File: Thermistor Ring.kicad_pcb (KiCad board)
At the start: 2 copper layers, 158.9 x 126.1 mm, 19 parts, among them J1 Conn_01x04_Socket, U1 TPS7A2018PDBVR, U2 MCP9808T-E/MC, U3 MCP9808T-E/MC, U4 MCP9808T-E/MC, U5 MCP9808T-E/MC, U6 MCP9808T-E/MC, U7 MCP9808T-E/MC

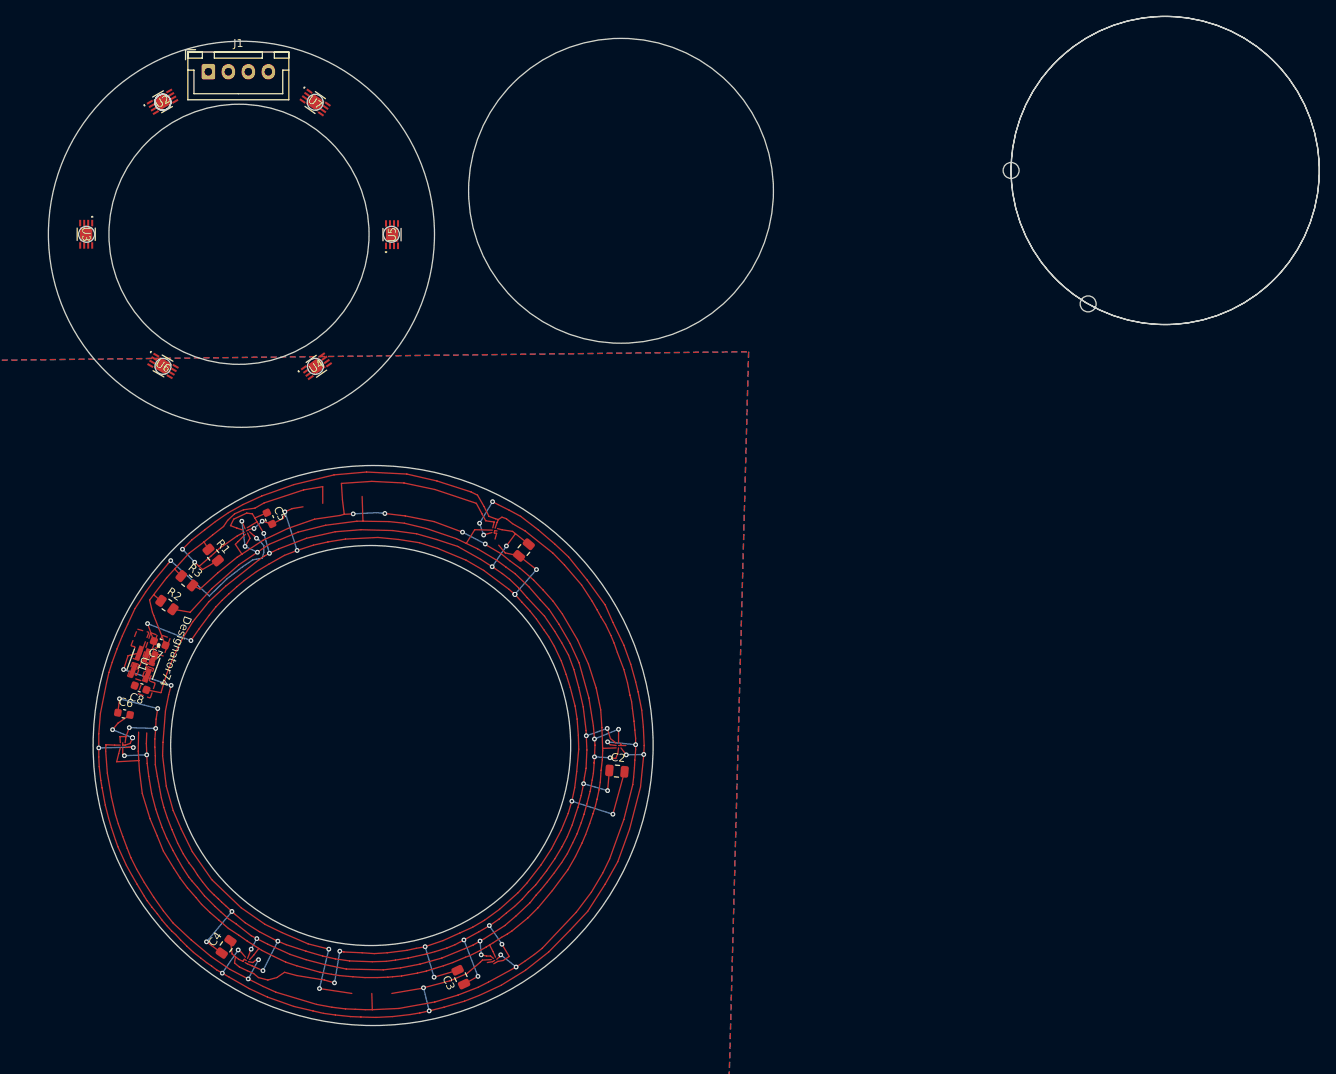
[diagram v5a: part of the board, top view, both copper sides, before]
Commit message: smaller ring first draft
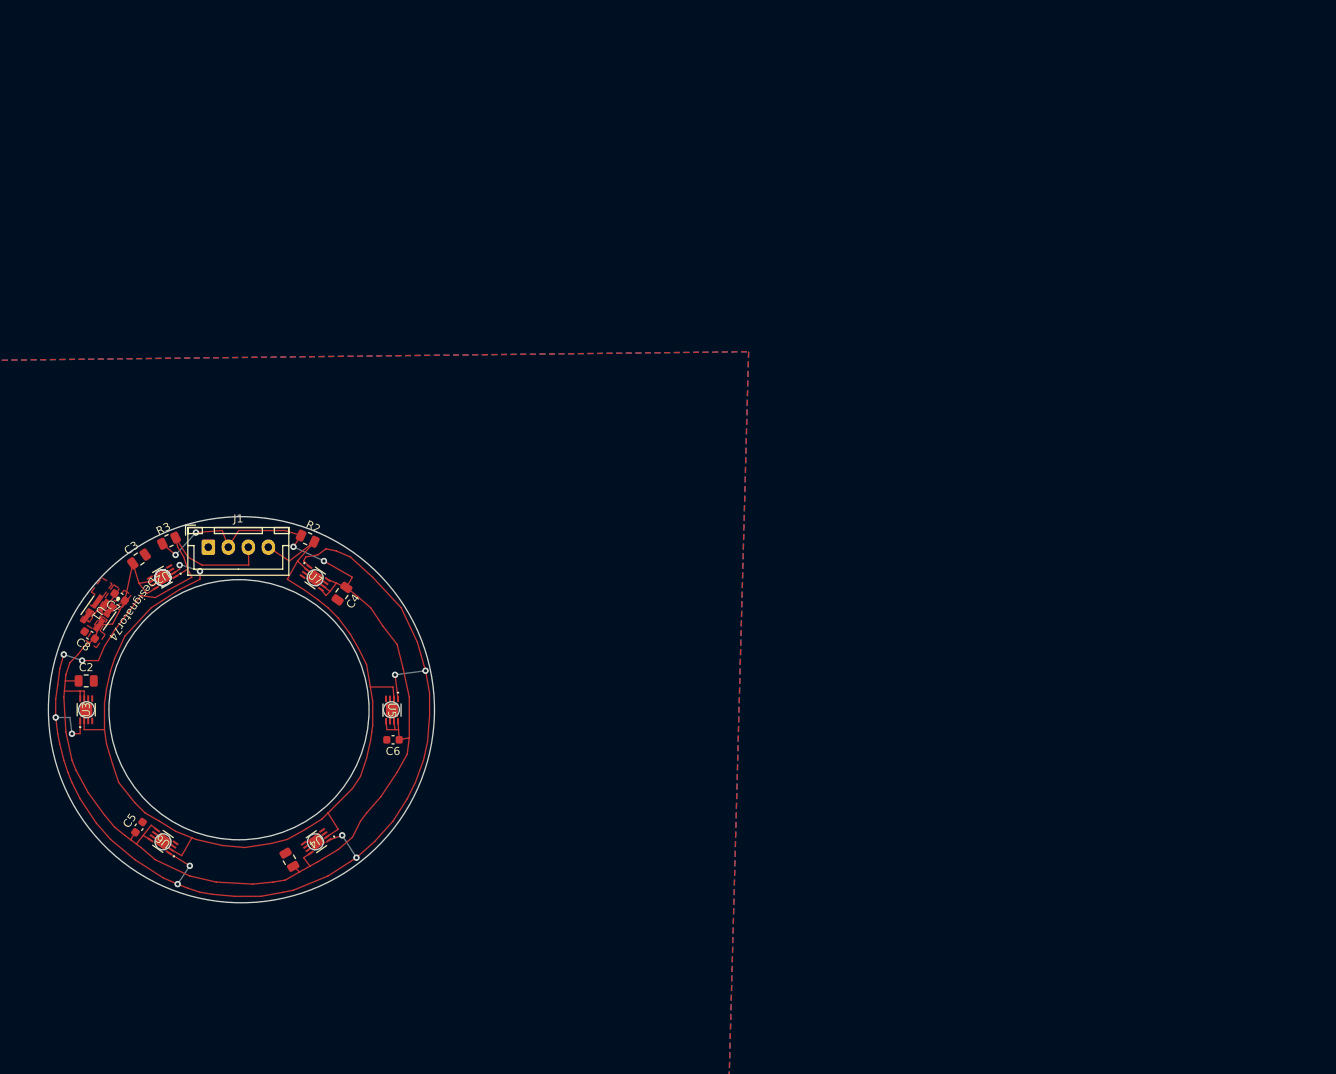
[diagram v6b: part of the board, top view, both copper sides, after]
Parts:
- removed R1: 4.7k, Resistor_SMD:R_0805_2012Metric
- moved C2 67.3 mm to (55.4, 52.1), turned to 0 degrees
- moved C3 66.0 mm to (62.0, 36.8), turned to 35 degrees
- moved U5 59.4 mm to (93.6, 55.7), turned to -90 degrees
- moved J1 59.4 mm to (70.6, 35.4)
- moved U2 59.4 mm to (64.9, 39.1), turned to -150 degrees
- moved U3 59.4 mm to (55.4, 55.7), turned to 90 degrees
- moved U6 59.4 mm to (65.0, 72.1), turned to 145 degrees
- moved U7 59.4 mm to (84.0, 39.2)
- moved U4 59.4 mm to (84.2, 72.2), turned to -145 degrees
- moved C1 48.6 mm to (80.8, 74.4), turned to 120 degrees
- moved C4 46.5 mm to (87.3, 41.2), turned to -125 degrees
- moved C5 41.9 mm to (62.0, 70.4), turned to 55 degrees
- moved C6 33.8 mm to (93.7, 59.4), turned to 180 degrees
- moved R2 19.4 mm to (83.1, 34.3), turned to -25 degrees
- moved C8 9.14 mm to (55.8, 46.3), turned to 145 degrees
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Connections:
- C5 pad 1: unconnected-(C5-Pad1) -> /Power 3.3-5V
- U2 pad 3: /INT -> unconnected-(U2-ALERT-Pad3)
- U3 pad 3: /INT -> unconnected-(U3-ALERT-Pad3)
- U4 pad 3: /INT -> unconnected-(U4-ALERT-Pad3)
- U5 pad 3: /INT -> unconnected-(U5-ALERT-Pad3)
- U6 pad 3: /INT -> unconnected-(U6-ALERT-Pad3)
- U7 pad 3: /INT -> unconnected-(U7-ALERT-Pad3)
- U7 pad 5: /SDA -> /Power 3.3-5V
- U7 pad 6: /SDA -> /Power 3.3-5V
- U7 pad 8: /SDA -> /Power 3.3-5V
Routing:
- net (no net): track 469.1 -> 0.00 mm, vias 13 -> 0
- net /INT: track 213.3 -> 0.00 mm, vias 8 -> 0
- net GND: track 195.9 -> 0.00 mm, vias 18 -> 0
- net /Power 3.3-5V: track 38.4 -> 179.9 mm, vias 20 -> 4
- net /SCL: track 196.8 -> 132.0 mm, vias 13 -> 2
- net /ENABLE: track 61.8 -> 0.00 mm, vias 4 -> 0
- net /SDA: track 202.3 -> 175.9 mm, vias 4 -> 10
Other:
- board size 158.9 x 126.1 mm -> 48.3 x 48.3 mm

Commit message: wip: some fixes
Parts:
- moved R3 0.98 mm to (66.5, 35.2), turned to -90 degrees
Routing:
- net /Power 3.3-5V: track 179.9 -> 192.3 mm, vias 4 -> 3
- net /SDA: track 175.9 -> 171.3 mm
- net /SCL: track 132.0 -> 128.0 mm
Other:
- outline, holes or cut-outs redrawn

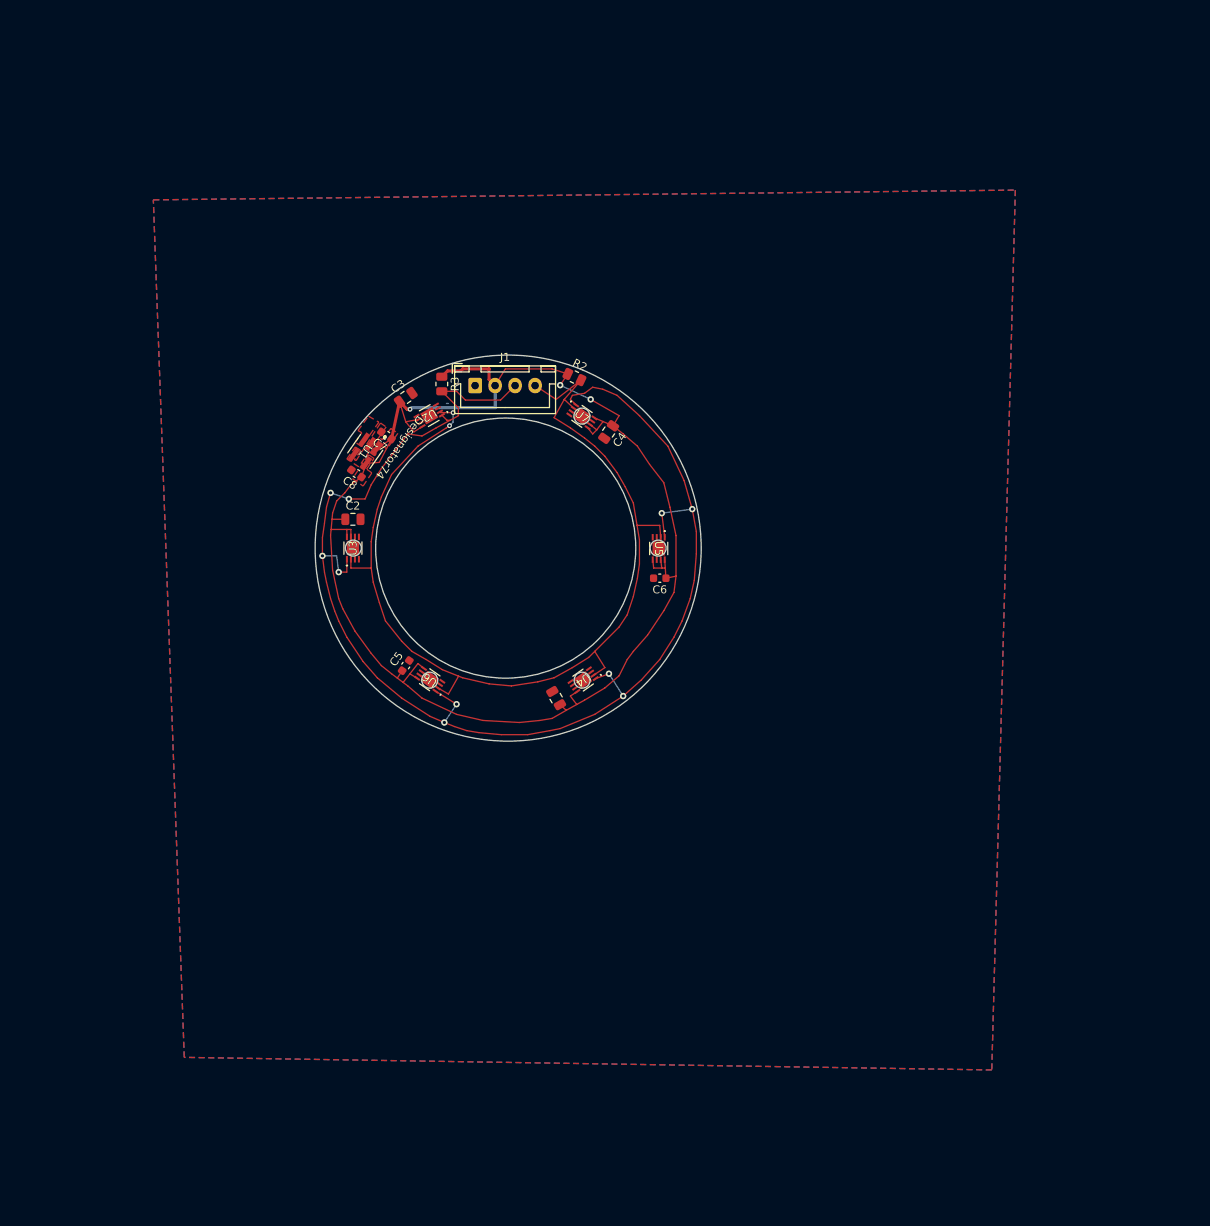
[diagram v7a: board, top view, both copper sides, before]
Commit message: Update PCB and resolve DRC
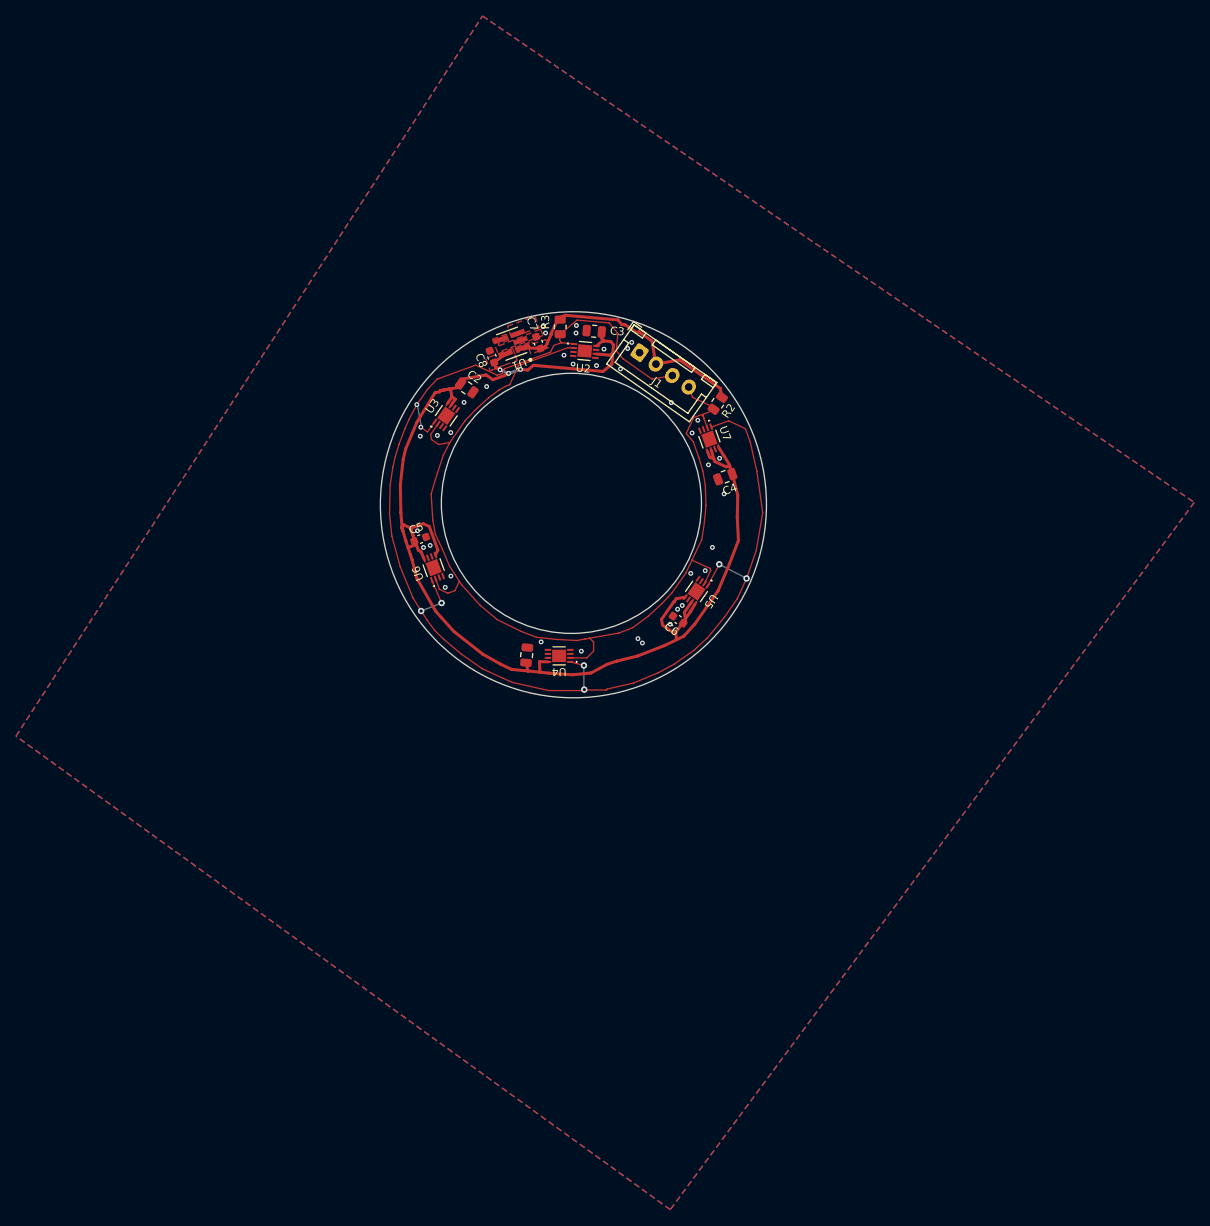
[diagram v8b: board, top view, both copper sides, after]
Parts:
- U1: footprint TPS7A201:DBV0005A-IPC_A -> TPS7A2018PDBVR:DBV0005A-IPC_A
- U2, U3, U4, U5, U6, U7: footprint mcp9808:DFN8_2x3MC_MCH -> MCP9808T-E:DFN8_2x3MC_MCH
- moved C3 25.0 mm to (85.5, 28.6), turned to 175 degrees
- moved U1 22.7 mm to (75.2, 30.1), turned to -160 degrees
- moved C8 22.4 mm to (72.7, 31.7), turned to 110 degrees
- moved C7 22.2 mm to (78.5, 30.0), turned to 110 degrees
- moved C2 21.7 mm to (69.6, 35.6), turned to -35 degrees
- moved U2 21.1 mm to (84.4, 31.0), turned to -5 degrees
- moved J1 21.0 mm to (91.2, 31.2), turned to -35 degrees
- moved U3 20.2 mm to (67.0, 39.1), turned to 55 degrees
- moved R2 18.2 mm to (101.0, 37.6), turned to -125 degrees
- moved R3 16.4 mm to (81.3, 28.0)
- moved U7 16.2 mm to (99.9, 42.1), turned to -70 degrees
- moved C5 15.9 mm to (63.8, 54.5), turned to 20 degrees
- moved C4 15.6 mm to (101.9, 46.7), turned to -160 degrees
- moved U6 14.0 mm to (65.5, 58.1), turned to 110 degrees
- moved U5 7.15 mm to (98.3, 61.1), turned to -125 degrees
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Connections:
- C1 pad 1: /Power 3.3-5V -> /VDD
- C2 pad 1: /Power 3.3-5V -> /VDD
- C3 pad 1: /Power 3.3-5V -> /VDD
- C4 pad 1: /Power 3.3-5V -> /VDD
- C5 pad 1: /Power 3.3-5V -> /VDD
- C6 pad 1: /Power 3.3-5V -> /VDD
- C8 pad 1: /Power 3.3-5V -> /VDD
- U1 pad 5: /Power 3.3-5V -> /VDD
- U2 pad 3: unconnected-(U2-ALERT-Pad3) -> GND
- U2 pad 5: unconnected-(U2-A2-Pad5) -> GND
- U2 pad 6: /Power 3.3-5V -> /VDD
- U2 pad 7: unconnected-(U2-A0-Pad7) -> GND
- U2 pad 8: /Power 3.3-5V -> /VDD
- U2 pad 9: unconnected-(U2-EPAD-Pad9) -> GND
- U3 pad 3: unconnected-(U3-ALERT-Pad3) -> GND
- U3 pad 5: unconnected-(U3-A2-Pad5) -> GND
- U3 pad 6: unconnected-(U3-A1-Pad6) -> GND
- U3 pad 7: /Power 3.3-5V -> /VDD
- U3 pad 8: /Power 3.3-5V -> /VDD
- U3 pad 9: unconnected-(U3-EPAD-Pad9) -> GND
- U4 pad 3: unconnected-(U4-ALERT-Pad3) -> GND
- U4 pad 5: unconnected-(U4-A2-Pad5) -> GND
- U4 pad 6: unconnected-(U4-A1-Pad6) -> GND
- U4 pad 7: unconnected-(U4-A0-Pad7) -> GND
- U4 pad 8: /Power 3.3-5V -> /VDD
- U5 pad 3: unconnected-(U5-ALERT-Pad3) -> GND
- U5 pad 5: /Power 3.3-5V -> /VDD
- U5 pad 6: unconnected-(U5-A1-Pad6) -> GND
- U5 pad 7: /Power 3.3-5V -> /VDD
- U5 pad 8: /Power 3.3-5V -> /VDD
- U5 pad 9: unconnected-(U5-EPAD-Pad9) -> GND
- U6 pad 3: unconnected-(U6-ALERT-Pad3) -> GND
- U6 pad 5: /Power 3.3-5V -> /VDD
- U6 pad 6: unconnected-(U6-A1-Pad6) -> GND
- U6 pad 7: unconnected-(U6-A0-Pad7) -> GND
- U6 pad 8: /Power 3.3-5V -> /VDD
- U6 pad 9: unconnected-(U6-EPAD-Pad9) -> GND
- U7 pad 3: unconnected-(U7-ALERT-Pad3) -> GND
- U7 pad 5: /Power 3.3-5V -> /VDD
- U7 pad 6: /Power 3.3-5V -> /VDD
- U7 pad 7: unconnected-(U7-A0-Pad7) -> GND
- U7 pad 8: /Power 3.3-5V -> /VDD
- U7 pad 9: unconnected-(U7-EPAD-Pad9) -> GND
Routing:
- net /VDD: track 0.00 -> 169.3 mm, vias 0 -> 3
- net /Power 3.3-5V: track 192.3 -> 32.8 mm, vias 3 -> 0
- net /SCL: track 128.0 -> 122.6 mm, vias 2 -> 0
- net /SDA: track 171.3 -> 167.4 mm, vias 10 -> 8
- net GND: vias 0 -> 37
- added copper zone on F.Cu, net /VDD
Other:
- outline, holes or cut-outs redrawn
